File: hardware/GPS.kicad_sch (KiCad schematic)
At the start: 24 parts, among them IC3 LDFPVR, J1 Conn_Coaxial, U3 NEO-M9N

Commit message: revised GPS chip with new TODO item
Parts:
- added IC4: NEO-M9V-20B, NEOM9V20B, symbol Loaded_Libraries:NEO-M9V-20B
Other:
- note added: "TODO: Implement this instead"
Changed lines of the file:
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@@
 		)
 	)
+	(text "TODO: Implement this instead"
+		(exclude_from_sim no)
+		(at 144.272 131.572 0)
+		(effects
+			(font
+				(size 2.286 2.286)
+			)
+		)
+	)
 	(text "reference"
 		(exclude_from_sim yes)
@@
 					(unit 1)
 				)
+			)
+		)
+	)
+	(symbol
+		(lib_id "Loaded_Libraries:NEO-M9V-20B")
+		(at 120.65 144.78 0)
+		(unit 1)
+		(body_style 1)
+		(exclude_from_sim no)
+		(in_bom yes)
+		(on_board yes)
+		(in_pos_files yes)
+		(dnp no)
+		(fields_autoplaced yes)
+		(property "Reference" "IC4"
+			(at 146.05 137.16 0)
+			(show_name no)
+			(do_not_autoplace no)
+			(effects
+				(font
+					(size 1.27 1.27)
+				)
+			)
+		)
+		(property "Value" "NEO-M9V-20B"
+			(at 146.05 139.7 0)
+			(show_name no)
+			(do_not_autoplace no)
+			(effects
+				(font
+					(size 1.27 1.27)
+				)
+			)
+		)
+		(property "Footprint" "NEOM9V20B"
+			(at 167.64 239.7 0)
+			(hide yes)
+			(show_name no)
+			(do_not_autoplace no)
+			(effects
+				(font
+					(size 1.27 1.27)
+				)
+				(justify left top)
+			)
+		)
+		(property "Datasheet" "https://content.u-blox.com/sites/default/files/NEO-M9V-20B_DataSheet_UBX-21029781.pdf"
+			(at 167.64 339.7 0)
+			(hide yes)
+			(show_name no)
+			(do_not_autoplace no)
+			(effects
+				(font
+					(size 1.27 1.27)
+				)
+				(justify left top)
+			)
+		)
+		(property "Description" "GPS Modules"
+			(at 120.65 144.78 0)
+			(hide yes)
+			(show_name no)
+			(do_not_autoplace no)
+			(effects
+				(font
+					(size 1.27 1.27)
+				)
+			)
+		)
+		(property "Height" "2.6"
+			(at 167.64 539.7 0)
+			(hide yes)
+			(show_name no)
+			(do_not_autoplace no)
+			(effects
+				(font
+					(size 1.27 1.27)
+				)
+				(justify left top)
+			)
+		)
+		(property "Mouser Part Number" "377-NEO-M9V-20B"
+			(at 167.64 639.7 0)
+			(hide yes)
+			(show_name no)
+			(do_not_autoplace no)
+			(effects
+				(font
+					(size 1.27 1.27)
+				)
+				(justify left top)
+			)
+		)
+		(property "Mouser Price/Stock" "https://www.mouser.co.uk/ProductDetail/u-blox/NEO-M9V-20B?qs=TCDPyi3sCW0wo5Ra8BoqwQ%3D%3D"
+			(at 167.64 739.7 0)
+			(hide yes)
+			(show_name no)
+			(do_not_autoplace no)
+			(effects
+				(font
+					(size 1.27 1.27)
+				)
+				(justify left top)
+			)
+		)
+		(property "Manufacturer_Name" "u-blox"
+			(at 167.64 839.7 0)
+			(hide yes)
+			(show_name no)
+			(do_not_autoplace no)
+			(effects
+				(font
+					(size 1.27 1.27)
+				)
+				(justify left top)
+			)
+		)
+		(property "Manufacturer_Part_Number" "NEO-M9V-20B"
+			(at 167.64 939.7 0)
+			(hide yes)
+			(show_name no)
+			(do_not_autoplace no)
+			(effects
+				(font
+					(size 1.27 1.27)
+				)
+				(justify left top)
+			)
+		)
+		(pin "13"
+		)
+		(pin "19"
+		)
+		(pin "5"
+		)
+		(pin "11"
+		)
+		(pin "3"
+		)
+		(pin "24"
+		)
+		(pin "6"
+		)
+		(pin "18"
+		)
+		(pin "2"
+		)
+		(pin "4"
+		)
+		(pin "8"
+		)
+		(pin "1"
+		)
+		(pin "15"
+		)
+		(pin "9"
+		)
+		(pin "10"
+		)
+		(pin "12"
+		)
+		(pin "16"
+		)
+		(pin "20"
+		)
+		(pin "21"
+		)
+		(pin "7"
+		)
+		(pin "14"
+		)
+		(pin "17"
+		)
+		(pin "23"
+		)
+		(pin "22"
+		)
+		(instances
+			(project "PTMS_INS"
+				(path "/7abec38e-2a6a-4c7d-a187-5990bacce22b/f942e906-05a7-458b-b36b-7481d7d3c3d2"
+					(reference "IC4")
+					(unit 1)
+				)

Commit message: migrate to impart gui, begin redo of imu schematic
add to symbol library: ImpartGUI |
${KICAD_3RD_PARTY}/ImpartGUI.kicad_sym | format KiCad. add to footprint
library: ImpartGUI | ${KICAD_3RD_PARTY}/ImpartGUI.pretty | KiCad
-This is a choice made to keep project portable at the cost of larger
repo size.
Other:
- moved on the sheet: IC4
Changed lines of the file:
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@@
 	(symbol
 		(lib_id "Loaded_Libraries:NEO-M9V-20B")
-		(at 120.65 144.78 0)
+		(at 120.65 143.51 0)
 		(unit 1)
 		(body_style 1)
@@
 		(fields_autoplaced yes)
 		(property "Reference" "IC4"
-			(at 146.05 137.16 0)
+			(at 146.05 135.89 0)
 			(show_name no)
 			(do_not_autoplace no)
@@
 		)
 		(property "Value" "NEO-M9V-20B"
-			(at 146.05 139.7 0)
+			(at 146.05 138.43 0)
 			(show_name no)
 			(do_not_autoplace no)
@@
 		)
 		(property "Footprint" "NEOM9V20B"
-			(at 167.64 239.7 0)
+			(at 167.64 238.43 0)
 			(hide yes)
 			(show_name no)
@@
 		)
 		(property "Datasheet" "https://content.u-blox.com/sites/default/files/NEO-M9V-20B_DataSheet_UBX-21029781.pdf"
-			(at 167.64 339.7 0)
+			(at 167.64 338.43 0)
 			(hide yes)
 			(show_name no)
@@
 		)
 		(property "Description" "GPS Modules"
-			(at 120.65 144.78 0)
+			(at 120.65 143.51 0)
 			(hide yes)
 			(show_name no)
@@
 		)
 		(property "Height" "2.6"
-			(at 167.64 539.7 0)
+			(at 167.64 538.43 0)
 			(hide yes)
 			(show_name no)
@@
 		)
 		(property "Mouser Part Number" "377-NEO-M9V-20B"
-			(at 167.64 639.7 0)
+			(at 167.64 638.43 0)
 			(hide yes)
 			(show_name no)
@@
 		)
 		(property "Mouser Price/Stock" "https://www.mouser.co.uk/ProductDetail/u-blox/NEO-M9V-20B?qs=TCDPyi3sCW0wo5Ra8BoqwQ%3D%3D"
-			(at 167.64 739.7 0)
+			(at 167.64 738.43 0)
 			(hide yes)
 			(show_name no)
@@
 		)
 		(property "Manufacturer_Name" "u-blox"
-			(at 167.64 839.7 0)
+			(at 167.64 838.43 0)
 			(hide yes)
 			(show_name no)
@@
 		)
 		(property "Manufacturer_Part_Number" "NEO-M9V-20B"
-			(at 167.64 939.7 0)
+			(at 167.64 938.43 0)
 			(hide yes)
 			(show_name no)

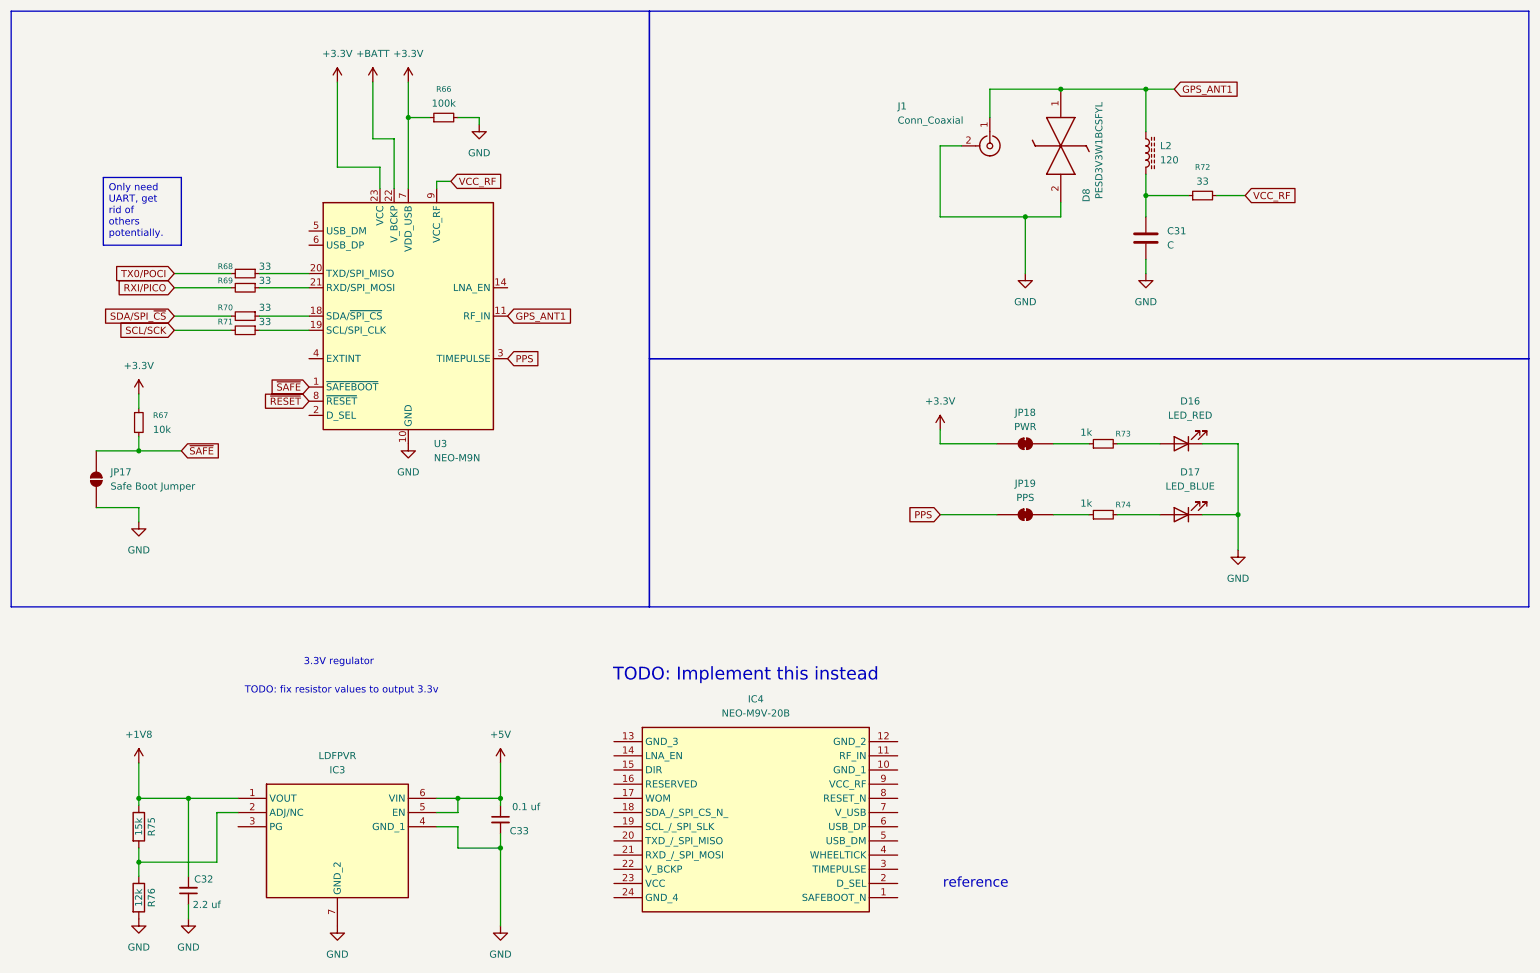
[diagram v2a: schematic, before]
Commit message: wire up altimeter, temp, barometer, imu, gps to MCU
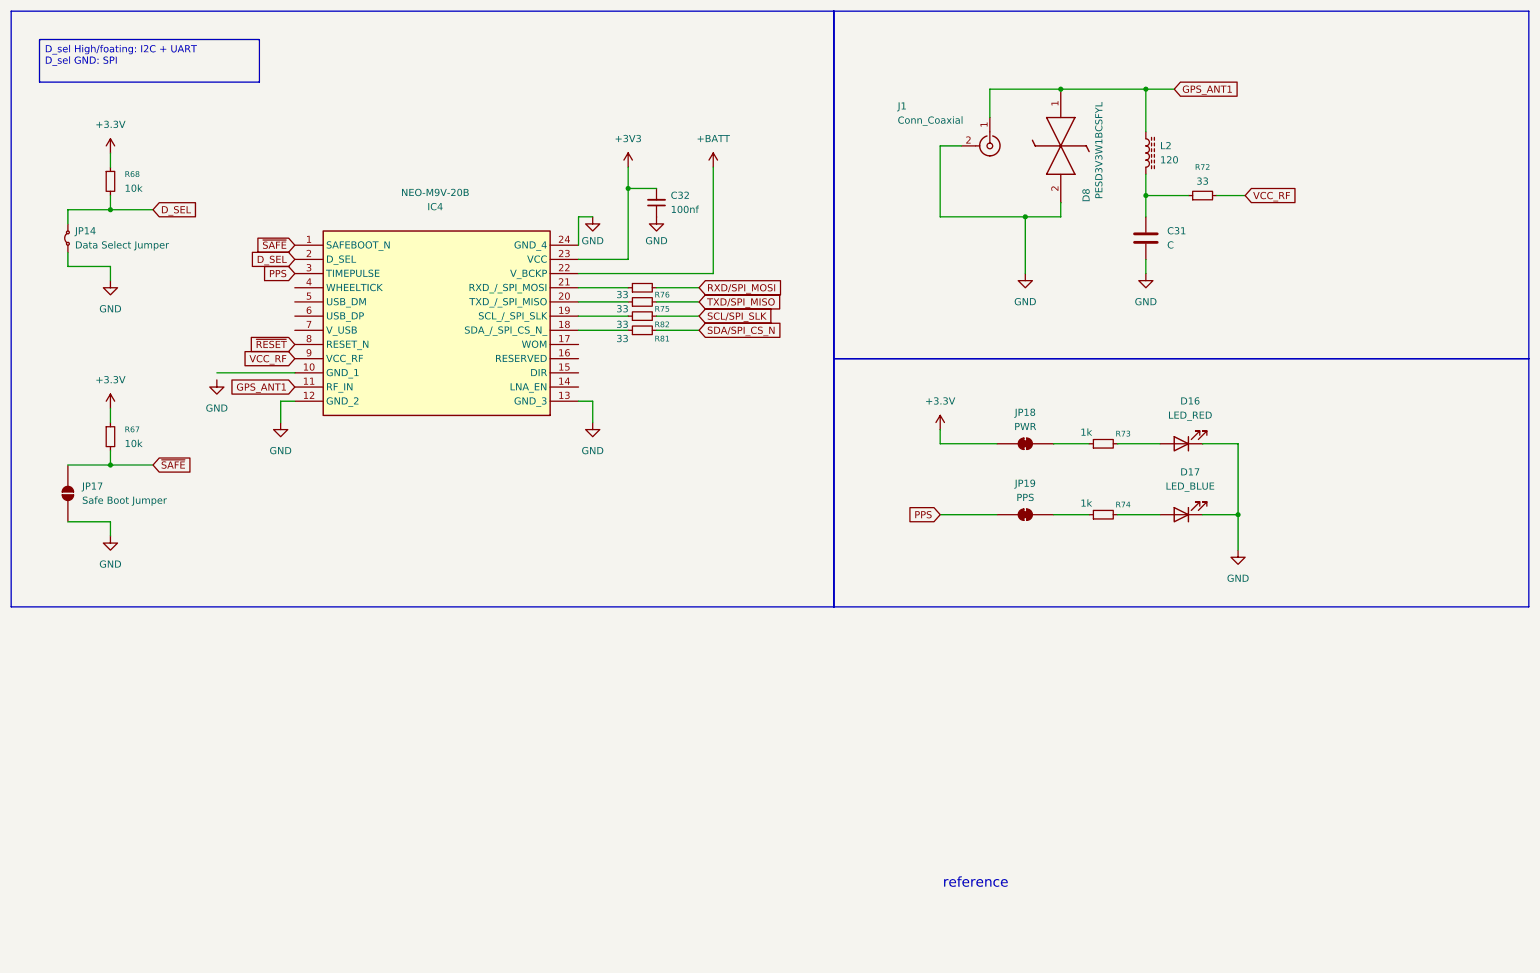
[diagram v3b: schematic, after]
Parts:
- removed C33: 0.1 uf, symbol Device:C_Small
- removed IC3: LDFPVR, SON65P200X200X100-7N-D, symbol Loaded_Libraries:LDFPVR
- removed R66: 100k, symbol Device:R_Small
- removed R69, R70, R71: 33, symbol Device:R_Small
- removed R75: 15k, symbol Device:R
- removed R76: 12k, symbol Device:R
- removed U3: NEO-M9N, RF_GPS:ublox_NEO, symbol RF_GPS:NEO-M9N
- added JP14: Data Select Jumper, symbol Jumper:Jumper_2_Small_Bridged
- added R75, R76, R81, R82: 33, symbol Device:R_Small
- C32: value 2.2 uf -> 100nf
- R68: value 33 -> 10k
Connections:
- net +1V8 is gone; now on net +3V3: C32.2
- net TX0/POCI is gone; now on net D_SEL: R68.2
- net +3.3V: now also R68.1
- net +BATT: now also IC4.22 (V_BCKP)
- net GND: now also IC4.12 (GND_2), IC4.13 (GND_3), IC4.24 (GND_4), JP14.1 (A)
- net GPS_ANT1: now also IC4.11 (RF_IN)
- net PPS: now also IC4.3 (TIMEPULSE)
- net VCC_RF: now also IC4.9 (VCC_RF)
- net ~{RESET}: now also IC4.8 (RESET_N)
- net ~{SAFE}: now also IC4.1 (SAFEBOOT_N)
- net at IC4.18 (SDA_/_SPI_CS_N_): now also R81.1
- net at IC4.19 (SCL_/_SPI_SLK): now also R82.1
- net D_SEL: now reaches IC4.2 (D_SEL)
- net D_SEL: now also JP14.2 (B)
- net at IC4.20 (TXD_/_SPI_MISO): now also R75.1
- net at IC4.21 (RXD_/_SPI_MOSI): now also R76.1
- net +3V3: now reaches IC4.23 (VCC)
- new net RXD/SPI_MOSI: R76.2
- new net SCL/SPI_SLK : R82.2
- new net SDA/SPI_CS_N: R81.2
- new net TXD/SPI_MISO: R75.2
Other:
- note removed: "3.3V regulator"
- note removed: "TODO: Implement this instead"
- note removed: "TODO: fix resistor values to output 3.3v"
- moved on the sheet: IC4, JP17, R67

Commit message: fixed electrical rules
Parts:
- added J2: Conn_02x02_Counter_Clockwise, symbol Connector_Generic:Conn_02x02_Counter_Clockwise
- IC4: footprint NEOM9V20B -> SamacSys_Parts:NEOM9V20B
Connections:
- net +3.3V is gone; now on net +3V3: JP18.1 (A), R67.1, R68.1
- net GND: now also IC4.10 (GND_1), J2.3 (Pin_3)
- net DIR_VEH: now reaches IC4.15 (DIR)
- net WAKE_ON_MOTION: now reaches IC4.17 (WOM)
- net WHEELTICK: now reaches IC4.4 (WHEELTICK)
- net USB_DM: now reaches IC4.5 (USB_DM)
- net USB_DM: now also J2.1 (Pin_1)
- net USBDP: now reaches IC4.6 (USB_DP)
- net USBDP: now also J2.2 (Pin_2)
- net V_USB: now reaches IC4.7 (V_USB)
- net V_USB: now also J2.4 (Pin_4)
- no-connect marks 0 -> 2
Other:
- note added: "usb header"
